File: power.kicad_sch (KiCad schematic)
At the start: 0 parts

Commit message: add P-FET and fuse for battery and bench
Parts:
- added F1, F2: 500mA, EasyEDA:F1206, symbol HAB5OBC:0466.500NRHF
- added Q1, Q2: AO3401A, EasyEDA:SOT-23_L2.9-W1.3-P1.90-LS2.4-BR, symbol HAB5OBC:AO3401A
- added R1, R2: 10k, EasyEDA:R0603, symbol HAB5OBC:0603WAF1002T5E
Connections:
- new net: F1.1, Q1.2 (S)
- new net: Q1.1 (G), R1.2
- new net: Q2.1 (G), R2.2
- new net: F2.1, Q2.2 (S)
- new net Battery_IN+: Q1.3 (D)
- new net Battery_IN-: R1.1
- new net Bench_IN+: Q2.3 (D)
- new net Bench_IN-: R2.1

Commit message: Add I2C, INA228 + accessories, and other small changes
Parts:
- added C1: 100nF, EasyEDA:C0603, symbol Device:C_Small
- added R3: 100mOhm, EasyEDA:R2512, symbol EasyEDA:LR2512-2AR100F4
- added U3: INA228AIDGSR, EasyEDA:VSSOP-10_L3.0-W3.0-P0.50-LS4.9-BL, symbol EasyEDA:INA228AIDGSR
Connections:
- net Bench_IN- is gone; now on net GND: R2.1
- net at F1.2: now also R3.1, U3.10 (IN+)
- net Battery_IN- renamed GND
- net GND: now also C1.1, U3.1 (A1), U3.2 (A0), U3.7 (GND)
- new net: R3.2, U3.8 (VBUS), U3.9 (IN–)
- new net +3.3V: C1.2, U3.6 (VS)
- new net I2C1.SCL: U3.5 (SCL)
- new net I2C1.SDA: U3.4 (SDA)
- no-connect marks 0 -> 1

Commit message: Added extra text for clarity
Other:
- note added: "Fuse"
- note added: "P-FET"
- note added: "Shunt"
- moved on the sheet: C1
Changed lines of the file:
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@@
 	(generator_version "10.0")
 	(paper "A4")
+	(text "P-FET\n"
+		(exclude_from_sim no)
+		(at 39.116 32.512 0)
+		(effects
+			(font
+				(size 1.27 1.27)
+				(thickness 0.254)
+				(bold yes)
+			)
+		)
+	)
+	(text "P-FET\n"
+		(exclude_from_sim no)
+		(at 39.37 61.722 0)
+		(effects
+			(font
+				(size 1.27 1.27)
+				(thickness 0.254)
+				(bold yes)
+			)
+		)
+	)
+	(text "Fuse\n"
+		(exclude_from_sim no)
+		(at 57.15 33.02 0)
+		(effects
+			(font
+				(size 1.27 1.27)
+				(thickness 0.254)
+				(bold yes)
+			)
+		)
+	)
+	(text "Fuse\n"
+		(exclude_from_sim no)
+		(at 57.404 61.722 0)
+		(effects
+			(font
+				(size 1.27 1.27)
+				(thickness 0.254)
+				(bold yes)
+			)
+		)
+	)
+	(text "Shunt\n"
+		(exclude_from_sim no)
+		(at 73.914 33.528 0)
+		(effects
+			(font
+				(size 1.27 1.27)
+				(thickness 0.254)
+				(bold yes)
+			)
+		)
+	)
 	(junction
 		(at 67.31 41.91)
@@
 	)
 	(junction
-		(at 80.01 16.51)
+		(at 85.09 16.51)
 		(diameter 0)
 		(color 0 0 0 0)
@@
 	)
 	(junction
-		(at 80.01 21.59)
+		(at 85.09 21.59)
 		(diameter 0)
 		(color 0 0 0 0)
@@
 	(wire
 		(pts
-			(xy 80.01 21.59) (xy 88.9 21.59)
+			(xy 85.09 21.59) (xy 88.9 21.59)
 		)
 		(stroke
@@
 	(wire
 		(pts
-			(xy 80.01 16.51) (xy 88.9 16.51)
+			(xy 85.09 16.51) (xy 88.9 16.51)
 		)
 		(stroke
@@
 	(symbol
 		(lib_id "power:+3.3V")
-		(at 80.01 16.51 0)
+		(at 85.09 16.51 0)
 		(unit 1)
 		(body_style 1)
@@
 		(dnp no)
 		(property "Reference" "#PWR06"
-			(at 80.01 20.32 0)
+			(at 85.09 20.32 0)
 			(hide yes)
 			(show_name no)
@@
 		)
 		(property "Value" "+3.3V"
-			(at 79.756 13.208 0)
+			(at 84.836 13.208 0)
 			(show_name no)
 			(do_not_autoplace no)
@@
 		)
 		(property "Footprint" "EasyEDA:R2512"
-			(at 80.01 16.51 0)
+			(at 85.09 16.51 0)
 			(hide yes)
 			(show_name no)
@@
 		)
 		(property "Datasheet" ""
-			(at 80.01 16.51 0)
+			(at 85.09 16.51 0)
 			(hide yes)
 			(show_name no)
@@
 		)
 		(property "Description" "Power symbol creates a global label with name \"+3.3V\""
-			(at 80.01 16.51 0)
+			(at 85.09 16.51 0)
 			(hide yes)
 			(show_name no)
@@
 	(symbol
 		(lib_id "power:GND")
-		(at 80.01 21.59 0)
+		(at 85.09 21.59 0)
 		(unit 1)
 		(body_style 1)
@@
 		(dnp no)
 		(property "Reference" "#PWR05"
-			(at 80.01 27.94 0)
+			(at 85.09 27.94 0)
 			(hide yes)
 			(show_name no)
@@
 		)
 		(property "Value" "GND"
-			(at 76.708 24.638 0)
+			(at 81.788 24.638 0)
 			(show_name no)
 			(do_not_autoplace no)
@@
 		)
 		(property "Footprint" "EasyEDA:R2512"
-			(at 80.01 21.59 0)
+			(at 85.09 21.59 0)
 			(hide yes)
 			(show_name no)
@@
 		)
 		(property "Datasheet" ""
-			(at 80.01 21.59 0)
+			(at 85.09 21.59 0)
 			(hide yes)
 			(show_name no)
@@
 		)
 		(property "Description" "Power symbol creates a global label with name \"GND\" , ground"
-			(at 80.01 21.59 0)
+			(at 85.09 21.59 0)
 			(hide yes)
 			(show_name no)
@@
 		(in_pos_files yes)
 		(dnp no)
-		(fields_autoplaced yes)
 		(property "Reference" "U3"
-			(at 100.33 11.43 0)
+			(at 100.33 13.208 0)
 			(show_name no)
 			(do_not_autoplace no)
@@
 		)
 		(property "Value" "INA228AIDGSR"
-			(at 100.33 13.97 0)
+			(at 100.33 15.24 0)
 			(show_name no)
 			(do_not_autoplace no)
@@
 	(symbol
 		(lib_id "Device:C_Small")
-		(at 80.01 19.05 180)
+		(at 85.09 19.05 180)
 		(unit 1)
 		(body_style 1)
@@
 		(dnp no)
 		(property "Reference" "C1"
-			(at 73.914 18.034 0)
+			(at 78.994 18.034 0)
 			(show_name no)
 			(do_not_autoplace no)
@@
 		)
 		(property "Value" "100nF"
-			(at 71.882 19.812 0)
+			(at 76.962 19.812 0)
 			(show_name no)
 			(do_not_autoplace no)
@@
 		)
 		(property "Footprint" "EasyEDA:C0603"
-			(at 80.01 19.05 0)
+			(at 85.09 19.05 0)
 			(hide yes)
 			(show_name no)
@@
 		)
 		(property "Datasheet" "https://lcsc.com/product-detail/Multilayer-Ceramic-Capacitors-MLCC-SMD-SMT_100nF-104-10-50V_C14663.html"
-			(at 80.01 19.05 0)
+			(at 85.09 19.05 0)
 			(hide yes)
 			(show_name no)
@@
 		)
 		(property "Description" "Unpolarized capacitor, small symbol"
-			(at 80.01 8.89 0)
+			(at 85.09 8.89 0)
 			(hide yes)
 			(show_name no)
@@
 		)
 		(property "Manufacturer" "YAGEO(国巨)"
-			(at 80.01 6.35 0)
+			(at 85.09 6.35 0)
 			(hide yes)
 			(show_name no)
@@
 		)
 		(property "MPN" "CC0603KRX7R9BB104"
-			(at 80.01 3.81 0)
+			(at 85.09 3.81 0)
 			(hide yes)
 			(show_name no)
@@
 		)
 		(property "LCSC Part" "C14663"
-			(at 80.01 1.27 0)
-			(hide yes)
-			(show_name no)
+			(at 85.09 1.27 0)
+			(hide yes)
+			(show_name no)

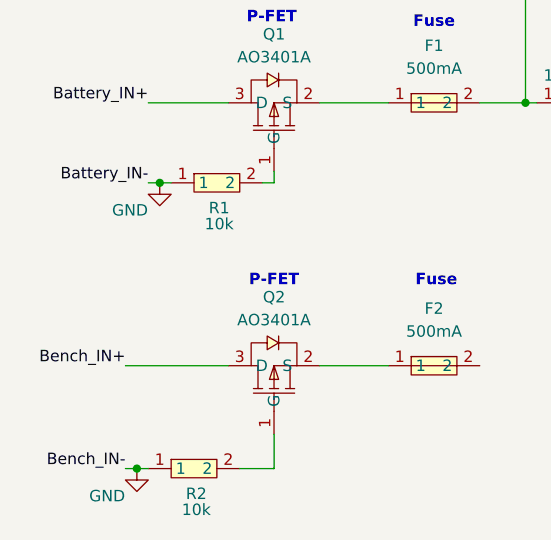
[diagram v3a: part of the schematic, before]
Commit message: new smaller resistor symbol
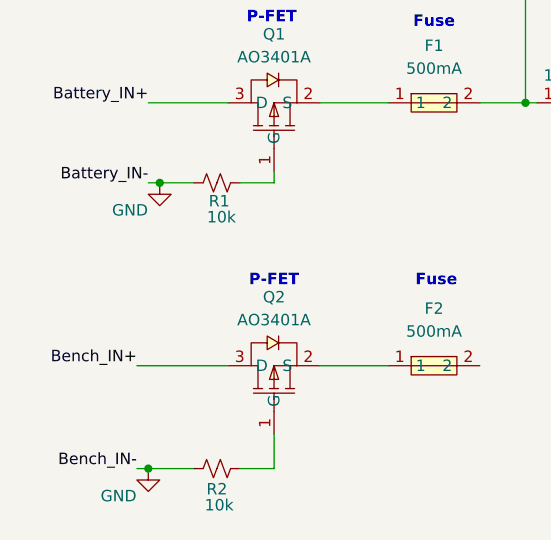
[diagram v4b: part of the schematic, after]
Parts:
- R1, R2: symbol HAB5OBC:0603WAF1002T5E -> Device:R_Small_US
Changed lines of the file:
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@@
 	)
 	(junction
-		(at 24.13 82.55)
+		(at 25.4 82.55)
 		(diameter 0)
 		(color 0 0 0 0)
@@
 	(wire
 		(pts
-			(xy 38.1 50.8) (xy 39.37 50.8)
-		)
-		(stroke
-			(width 0)
-			(type default)
-		)
-	)
-	(wire
-		(pts
 			(xy 114.3 30.48) (xy 114.3 29.21)
 		)
@@
 	(wire
 		(pts
-			(xy 26.67 50.8) (xy 27.94 50.8)
-		)
-		(stroke
-			(width 0)
-			(type default)
-		)
-	)
-	(wire
-		(pts
-			(xy 22.86 71.12) (xy 34.29 71.12)
+			(xy 26.67 50.8) (xy 30.48 50.8)
+		)
+		(stroke
+			(width 0)
+			(type default)
+		)
+	)
+	(wire
+		(pts
+			(xy 24.13 71.12) (xy 34.29 71.12)
 		)
 		(stroke
@@
 	(wire
 		(pts
-			(xy 24.13 82.55) (xy 22.86 82.55)
+			(xy 25.4 82.55) (xy 24.13 82.55)
 		)
 		(stroke
@@
 	(wire
 		(pts
-			(xy 25.4 82.55) (xy 24.13 82.55)
+			(xy 30.48 82.55) (xy 25.4 82.55)
 		)
 		(stroke
@@
 		(pts
 			(xy 111.76 19.05) (xy 124.46 19.05)
+		)
+		(stroke
+			(width 0)
+			(type default)
+		)
+	)
+	(wire
+		(pts
+			(xy 35.56 50.8) (xy 39.37 50.8)
 		)
 		(stroke
@@
 	)
 	(label "Bench_IN-"
-		(at 22.86 82.55 180)
+		(at 24.13 82.55 180)
 		(effects
 			(font
@@
 	)
 	(label "Bench_IN+"
-		(at 22.86 71.12 180)
+		(at 24.13 71.12 180)
 		(effects
 			(font
@@
 	(symbol
 		(lib_id "power:GND")
-		(at 24.13 82.55 0)
+		(at 25.4 82.55 0)
 		(unit 1)
 		(body_style 1)
@@
 		(dnp no)
 		(property "Reference" "#PWR09"
-			(at 24.13 88.9 0)
+			(at 25.4 88.9 0)
 			(hide yes)
 			(show_name no)
@@
 		)
 		(property "Value" "GND"
-			(at 20.828 85.598 0)
+			(at 22.098 85.598 0)
 			(show_name no)
 			(do_not_autoplace no)
@@
 		)
 		(property "Footprint" "EasyEDA:R2512"
-			(at 24.13 82.55 0)
+			(at 25.4 82.55 0)
 			(hide yes)
 			(show_name no)
@@
 		)
 		(property "Datasheet" ""
-			(at 24.13 82.55 0)
+			(at 25.4 82.55 0)
 			(hide yes)
 			(show_name no)
@@
 		)
 		(property "Description" "Power symbol creates a global label with name \"GND\" , ground"
-			(at 24.13 82.55 0)
+			(at 25.4 82.55 0)
 			(hide yes)
 			(show_name no)
@@
 	)
 	(symbol
-		(lib_id "HAB5OBC:0603WAF1002T5E")
-		(at 30.48 82.55 0)
+		(lib_id "Device:R_Small_US")
+		(at 33.02 82.55 90)
 		(unit 1)
 		(body_style 1)
@@
 		(dnp no)
 		(property "Reference" "R2"
-			(at 30.734 85.344 0)
+			(at 33.02 84.836 90)
 			(show_name no)
 			(do_not_autoplace no)
@@
 		)
 		(property "Value" "10k"
-			(at 30.734 87.122 0)
+			(at 33.274 86.614 90)
 			(show_name no)
 			(do_not_autoplace no)
@@
 		)
 		(property "Footprint" "EasyEDA:R0603"
-			(at 30.48 90.17 0)
+			(at 33.02 82.55 0)
 			(hide yes)
 			(show_name no)
@@
 		)
 		(property "Datasheet" "https://lcsc.com/product-detail/Chip-Resistor-Surface-Mount-UniOhm_10KR-1002-1_C25804.html"
-			(at 30.48 92.71 0)
-			(hide yes)
-			(show_name no)
-			(do_not_autoplace no)
-			(effects
-				(font
-					(size 1.27 1.27)
-				)
-			)
-		)
-		(property "Description" "10KΩ (1002) ±1%"
-			(at 30.48 105.41 0)
+			(at 33.02 82.55 0)
+			(hide yes)
+			(show_name no)
+			(do_not_autoplace no)
+			(effects
+				(font
+					(size 1.27 1.27)
+				)
+			)
+		)
+		(property "Description" "Resistor, small US symbol"
+			(at 33.02 82.55 0)
 			(hide yes)
 			(show_name no)
@@
 		)
 		(property "Manufacturer" "UNI-ROYAL(厚声)"
-			(at 30.48 95.25 0)
+			(at 45.72 82.55 0)
 			(hide yes)
 			(show_name no)
@@
 		)
 		(property "MPN" "0603WAF1002T5E"
-			(at 30.48 97.79 0)
+			(at 48.26 82.55 0)
 			(hide yes)
 			(show_name no)
@@
 		)
 		(property "LCSC Part" "C25804"
-			(at 30.48 100.33 0)
+			(at 50.8 82.55 0)
 			(hide yes)
 			(show_name no)
@@
 	)
 	(symbol
-		(lib_id "HAB5OBC:0603WAF1002T5E")
-		(at 33.02 50.8 0)
+		(lib_id "Device:R_Small_US")
+		(at 33.02 50.8 90)
 		(unit 1)
 		(body_style 1)
@@
 		(dnp no)
 		(property "Reference" "R1"
-			(at 33.274 53.594 0)
+			(at 33.274 52.832 90)
 			(show_name no)
 			(do_not_autoplace no)
@@
 		)
 		(property "Value" "10k"
-			(at 33.274 55.372 0)
+			(at 33.528 54.61 90)
 			(show_name no)
 			(do_not_autoplace no)
@@
 		)
 		(property "Footprint" "EasyEDA:R0603"
-			(at 33.02 58.42 0)
+			(at 33.02 50.8 0)
 			(hide yes)
 			(show_name no)
@@
 		)
 		(property "Datasheet" "https://lcsc.com/product-detail/Chip-Resistor-Surface-Mount-UniOhm_10KR-1002-1_C25804.html"
-			(at 33.02 60.96 0)
-			(hide yes)
-			(show_name no)
-			(do_not_autoplace no)
-			(effects
-				(font
-					(size 1.27 1.27)
-				)
-			)
-		)
-		(property "Description" "10KΩ (1002) ±1%"
-			(at 33.02 73.66 0)
+			(at 33.02 50.8 0)
+			(hide yes)
+			(show_name no)
+			(do_not_autoplace no)
+			(effects
+				(font
+					(size 1.27 1.27)
+				)
+			)
+		)
+		(property "Description" "Resistor, small US symbol"
+			(at 33.02 50.8 0)
 			(hide yes)
 			(show_name no)
@@
 		)
 		(property "Manufacturer" "UNI-ROYAL(厚声)"
-			(at 33.02 63.5 0)
+			(at 45.72 50.8 0)
 			(hide yes)
 			(show_name no)
@@
 		)
 		(property "MPN" "0603WAF1002T5E"
-			(at 33.02 66.04 0)
+			(at 48.26 50.8 0)
 			(hide yes)
 			(show_name no)
@@
 		)
 		(property "LCSC Part" "C25804"
-			(at 33.02 68.58 0)
-			(hide yes)
-			(show_name no)
+			(at 50.8 50.8 0)
+			(hide yes)
+			(show_name no)

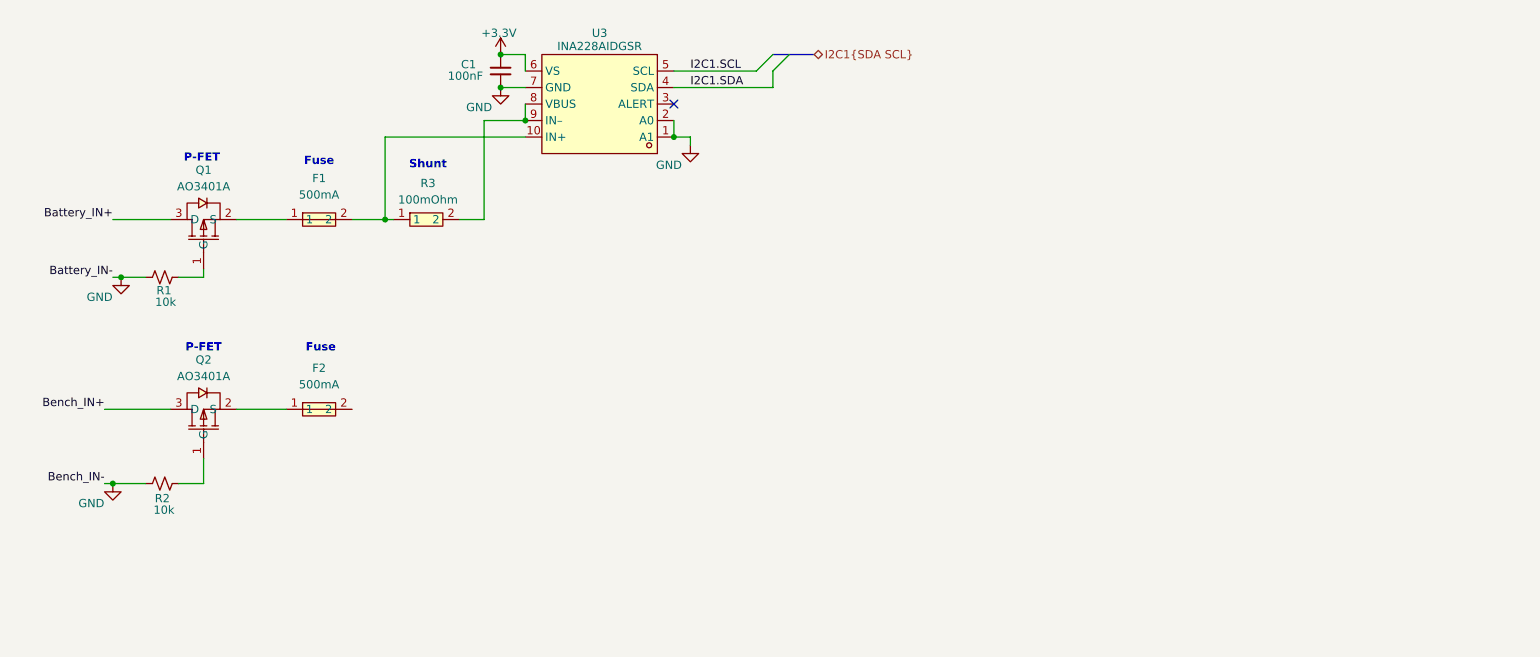
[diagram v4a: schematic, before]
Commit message: power2
Added LDO and MUX
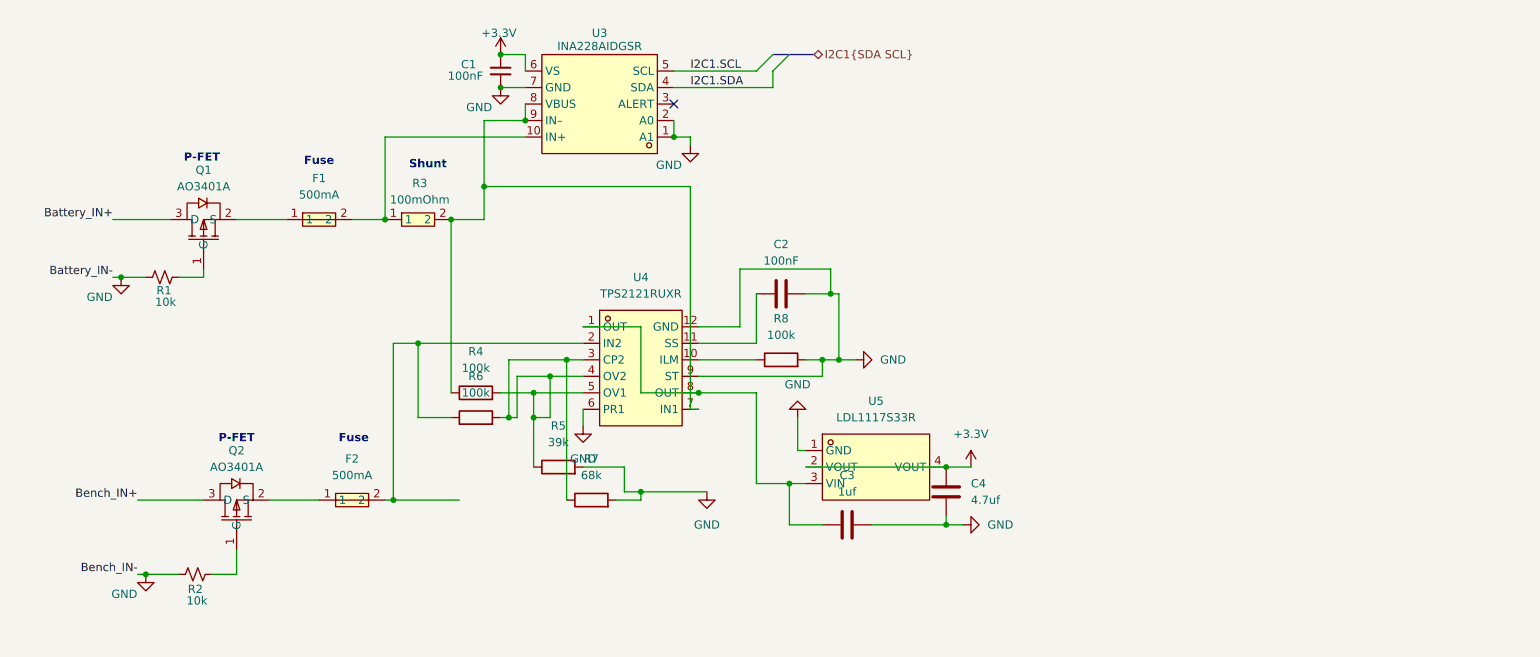
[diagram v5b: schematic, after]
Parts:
- added C2: 100nF, symbol Device:C
- added C3: 1uf, symbol Device:C
- added C4: 4.7uf, symbol Device:C
- added R4, R6, R8: 100k, symbol Device:R
- added R5: 39k, symbol Device:R
- added R7: 68k, symbol Device:R
- added U4: TPS2121RUXR, EasyEDA:VQFN-HR-12_L2.5-W2.0-P0.50-BL, symbol EasyEDA:TPS2121RUXR
- added U5: LDL1117S33R, EasyEDA:SOT-223-4_L6.5-W3.5-P2.30-LS7.0-BR, symbol EasyEDA:LDL1117S33R
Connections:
- net +3.3V: now also C4.2, U5.2 (VOUT), U5.4 (VOUT)
- net GND: now also C2.2, C3.2, C4.1, R5.2, R7.2, R8.2, U4.12 (GND), U4.6 (PR1), U4.9 (ST), U5.1 (GND)
- net at R3.2, U3.8 (VBUS), U3.9 (IN–): now also R4.1, U4.7 (IN1)
- net at F2.2: now also R6.1, U4.2 (IN2)
- new net: C3.1, U4.1 (OUT), U4.8 (OUT), U5.3 (VIN)
- new net: R8.1, U4.10 (ILM)
- new net: C2.1, U4.11 (SS)
- new net: R4.2, R5.1, R6.2, R7.1, U4.3 (CP2), U4.4 (OV2), U4.5 (OV1)
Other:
- moved on the sheet: F2, Q2, R2, R3

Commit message: rearrange mux resistors and new power bypass
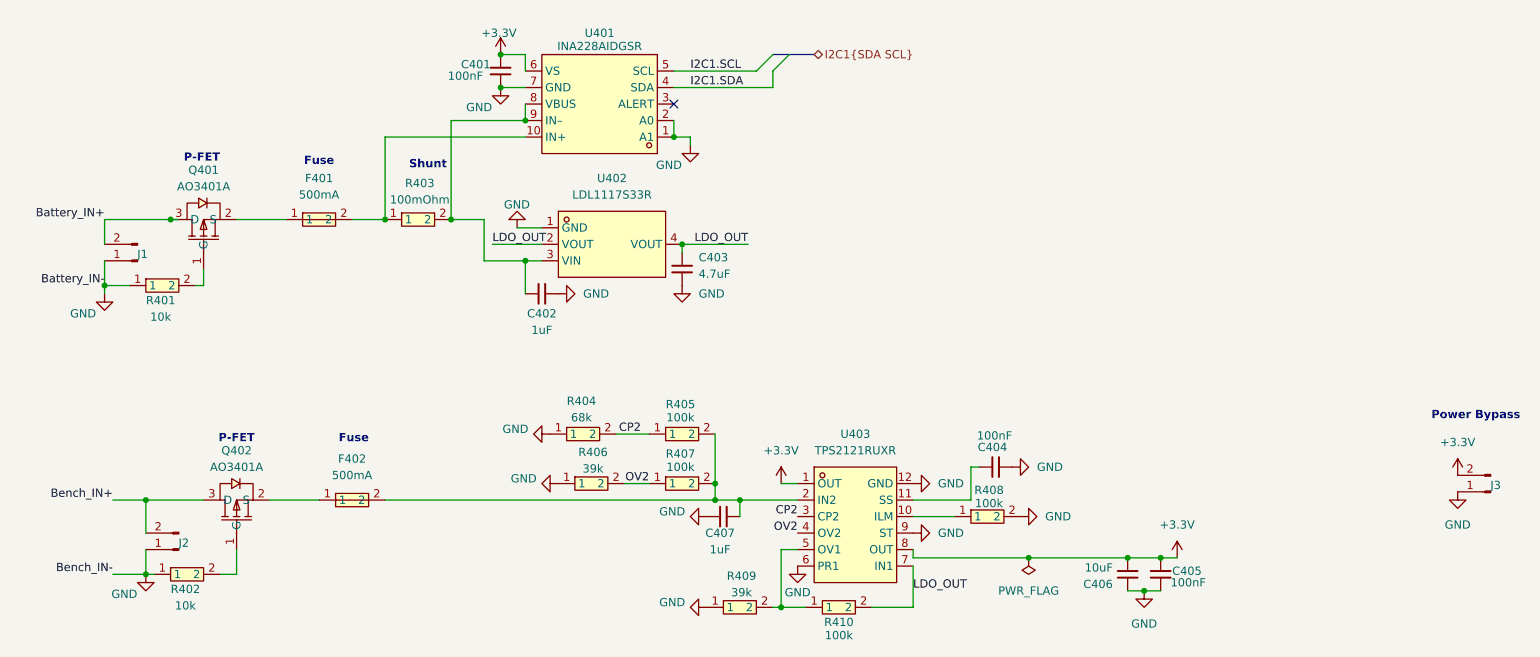
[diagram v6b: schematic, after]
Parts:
- removed C2: 100nF, symbol Device:C
- removed C3: 1uf, symbol Device:C
- removed C4: 4.7uf, symbol Device:C
- removed R1, R2: 10k, EasyEDA:R0603, symbol Device:R_Small_US
- removed R4, R6, R8: 100k, symbol Device:R
- removed R5: 39k, symbol Device:R
- removed R7: 68k, symbol Device:R
- added C402, C407: 1uF, EasyEDA:C0805, symbol Device:C_Small
- added C403: 4.7uF, EasyEDA:C1206, symbol Device:C_Small
- added C404, C405: 100nF, EasyEDA:C0603, symbol Device:C_Small
- added C406: 10uF, EasyEDA:C0805, symbol Device:C_Small
- added J1: (no value), symbol Connector:Conn_01x02_Pin
- added J2, J3: (no value), Connector_PinHeader_2.54mm:PinHeader_1x02_P2.54mm_Vertical, symbol Connector:Conn_01x02_Pin
- added R401, R402: 10k, EasyEDA:R0603, symbol HAB5OBC:0603WAF1002T5E
- added R404: 68k, EasyEDA:R0603, symbol HAB5OBC:0603WAF6802T5E
- added R405, R407, R408, R410: 100k, EasyEDA:R0603, symbol HAB5OBC:0603WAF1003T5E
- added R406, R409: 39k, EasyEDA:R0603, symbol HAB5OBC:0603WAF3902T5E
- renumbered C1 to C401, F1 to F401, F2 to F402, Q1 to Q401, Q2 to Q402, R3 to R403, U3 to U401, U5 to U402, U4 to U403
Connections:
- net +3.3V: now also U403.1 (OUT), U403.8 (OUT), C405.1, C406.1, J3.2 (Pin_2); no longer U402.2 (VOUT), U402.4 (VOUT)
- net Battery_IN+: now also J1.2 (Pin_2)
- net Bench_IN+: now also J2.2 (Pin_2)
- net GND: now also C402.1, C403.1, C404.1, C405.2, C406.2, C407.1, J1.1 (Pin_1), J2.1 (Pin_1), J3.1 (Pin_1), R401.1, R402.1, R404.1, R406.1, R408.2, R409.1
- net at U403.10 (ILM): now also R408.1
- net at U403.11 (SS): now also C404.2
- net at F402.2, U403.2 (IN2): now also C407.2, R405.2, R407.2
- net at R403.2, U401.8 (VBUS), U401.9 (IN–): now also U402.3 (VIN), C402.2; no longer U403.7 (IN1)
- net at Q401.1 (G): now also R401.2
- net at Q402.1 (G): now also R402.2
- new net: R409.2, R410.1, U403.5 (OV1)
- new net CP2: R404.2, R405.1, U403.3 (CP2)
- new net LDO_OUT: C403.2, R410.2, U402.2 (VOUT), U402.4 (VOUT), U403.7 (IN1)
- new net OV2: R406.2, R407.1, U403.4 (OV2)
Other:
- note added: "Power Bypass"
- moved on the sheet: U402, U403

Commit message: fix power to use correct symbol
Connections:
- net +3.3V renamed +3V3
